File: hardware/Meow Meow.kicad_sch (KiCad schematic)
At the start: 33 parts

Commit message: update layout
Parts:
- removed C?: 1uF, Capacitor_SMD:C_0603_1608Metric, symbol Meow-Meow-rescue:C_Small-MeowMeow-Meow-Meow-rescue-Meow-Meow-rescue-Meow-Meow-r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
- removed C?: 0.1uF, Capacitor_SMD:C_0603_1608Metric, symbol Meow-Meow-rescue:C_Small-MeowMeow-Meow-Meow-rescue-Meow-Meow-rescue-Meow-Meow-r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
- removed L?: 50Ω at 20MHz and 220Ω at 100MHz, symbol Device:L
- L1: renamed from L?; LCSC# (none) -> C85840
- gave numbers to parts that had none: 2
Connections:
- net GPIO05: now also U1.29 (PA20), U3.29 (PA20); no longer U1.30 (PA21), U3.30 (PA21)
- net GPIO06: now also U1.30 (PA21), U3.30 (PA21); no longer U1.29 (PA20), U3.29 (PA20)
- net GPIO10: now also U1.23 (PA14), U3.23 (PA14); no longer U1.20 (PB11), U3.20 (PB11)
- net GPIO11: now also U1.20 (PB11), U3.20 (PB11); no longer U1.23 (PA14), U3.23 (PA14)
- net VDDCORE: now reaches C1.1, U3.41 (VDDCORE)
- net VDDCORE: now also U1.41 (VDDCORE)
- net VDDANA: now reaches U1.6 (VDDANA)
- net VDDANA: now also L1.2, U3.6 (VDDANA)
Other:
- note added: "GPIO5 change to GPIO6"

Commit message: update version
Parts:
- C1: value (none) -> 1uF; footprint (none) -> Capacitor_SMD:C_0603_1608Metric
- C2, C7: value (none) -> 0.1uF; footprint (none) -> Capacitor_SMD:C_0603_1608Metric
- C4, C6: value (none) -> 10uF; footprint (none) -> Capacitors_SMD:C_0805_HandSoldering
- C5: value (none) -> 0.1uF; footprint (none) -> Capacitors_SMD:C_0805_HandSoldering
- D1: value (none) -> POWER; footprint (none) -> LEDs:LED_0805_HandSoldering
- D2: value (none) -> LED; footprint (none) -> LEDs:LED_0805_HandSoldering
- F1: value (none) -> 0.5A; footprint (none) -> Resistors_SMD:R_1812_HandSoldering
- J1: value (none) -> Conn_Left; footprint (none) -> Connector_PinSocket_2.54mm:PinSocket_1x16_P2.54mm_Vertical_SMD_Pin1Left
- J2: value (none) -> Conn_Right; footprint (none) -> Connector_PinSocket_2.54mm:PinSocket_1x12_P2.54mm_Vertical_SMD_Pin1Right
- J3: value (none) -> Conn_01x06; footprint (none) -> Connector:Tag-Connect_TC2030-IDC-NL_2x03_P1.27mm_Vertical
- L1: value (none) -> 50Ω at 20MHz and 220Ω at 100MHz; footprint (none) -> Inductor_SMD:L_0805_2012Metric
- P1: value (none) -> SPACE; footprint (none) -> Connectors_EC:SEWALLI_renew
- P10: value (none) -> A; footprint (none) -> Connectors_EC:SEWALLI_renew
- P11: value (none) -> W; footprint (none) -> Connectors_EC:SEWALLI_renew
- P12: value (none) -> KEY_UP_ARROW; footprint (none) -> Connectors_EC:SEWALLI_renew
- P2: value (none) -> KEY_DOWN_ARROW; footprint (none) -> Connectors_EC:SEWALLI_renew
- P3: value (none) -> KEY_RIGHT_ARROW; footprint (none) -> Connectors_EC:SEWALLI_renew
- P5: value (none) -> KEY_LEFT_ARROW; footprint (none) -> Connectors_EC:SEWALLI_renew
- P6: value (none) -> D; footprint (none) -> Connectors_EC:SEWALLI_renew
- P7: value (none) -> S; footprint (none) -> Connectors_EC:SEWALLI_renew
- P8: value (none) -> MOUSE_LEFT; footprint (none) -> Connectors_EC:SEWALLI_renew
- P9: value (none) -> USB_Micro; footprint (none) -> Connectors:U254051N4BH806
- R2, R3: value (none) -> 1K; footprint (none) -> Resistors_SMD:R_0805_HandSoldering
- SW1: value (none) -> RESET; footprint (none) -> Buttons_Switches_SMD:SW_SPST_TL3342
- U1: value (none) -> ATSAML21G18B-MUT; footprint (none) -> Package_DFN_QFN:QFN-48-1EP_7x7mm_P0.5mm_EP5.15x5.15mm; DNP (none) -> YES; manf# (none) -> ATSAML21G18B-MUT
- U2: value (none) -> AP2114-HA; footprint (none) -> Package_TO_SOT_SMD:SOT-223
- U3: value (none) -> ATSAML21G18B-AUT; footprint (none) -> Package_QFP:TQFP-48_7x7mm_P0.5mm; manf# (none) -> ATSAML21G18B-AUT

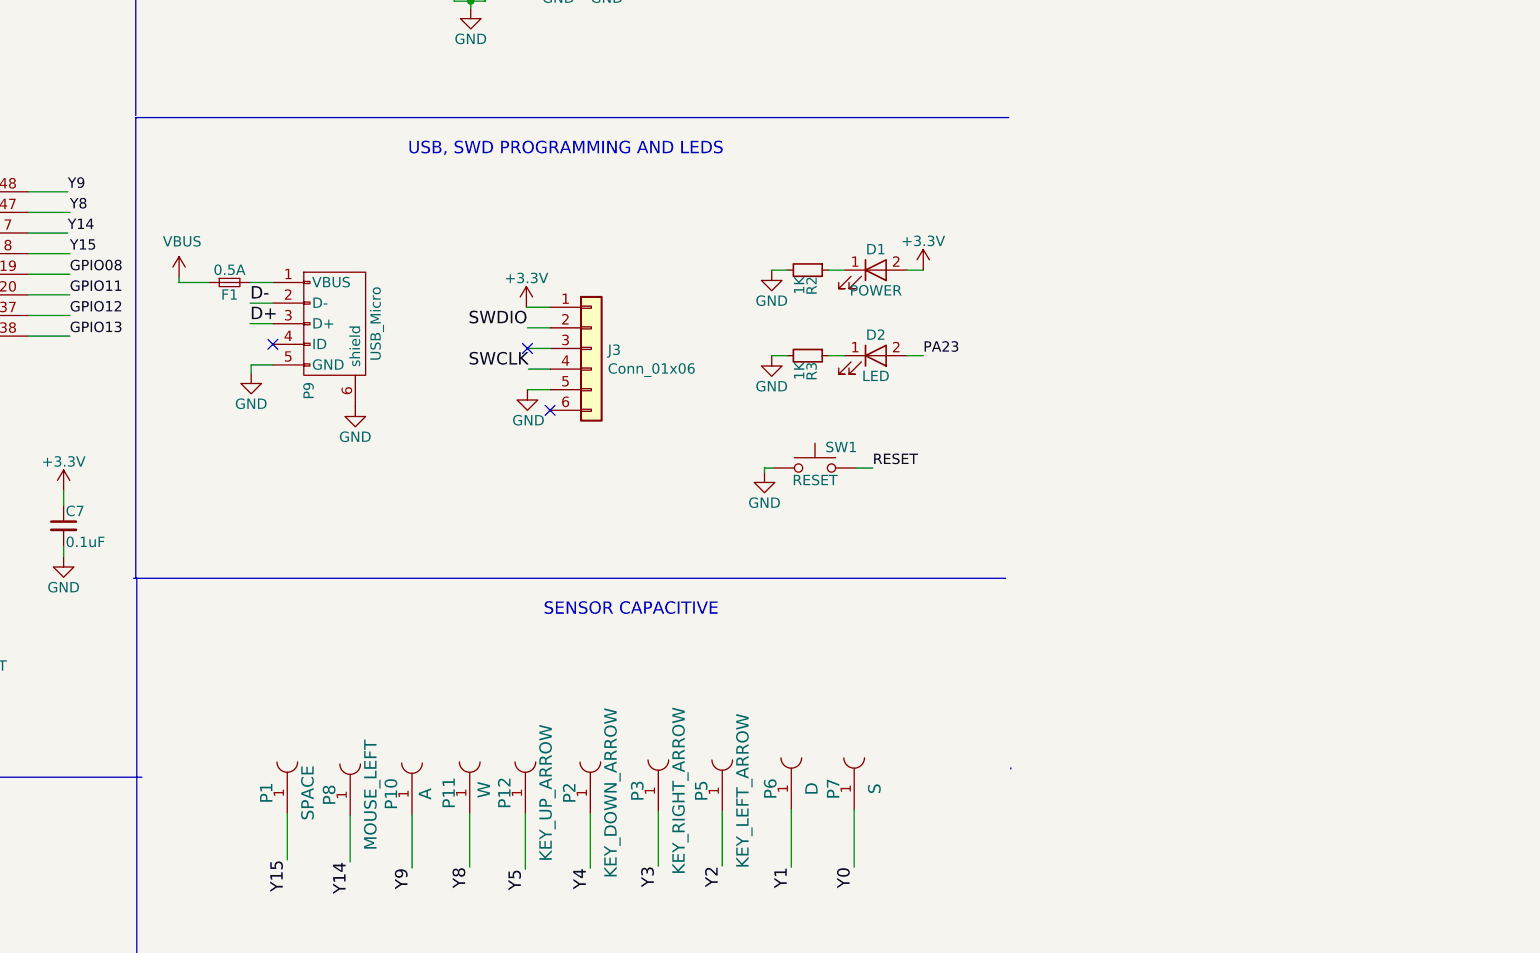
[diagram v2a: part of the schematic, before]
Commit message: update USB connector v3.1
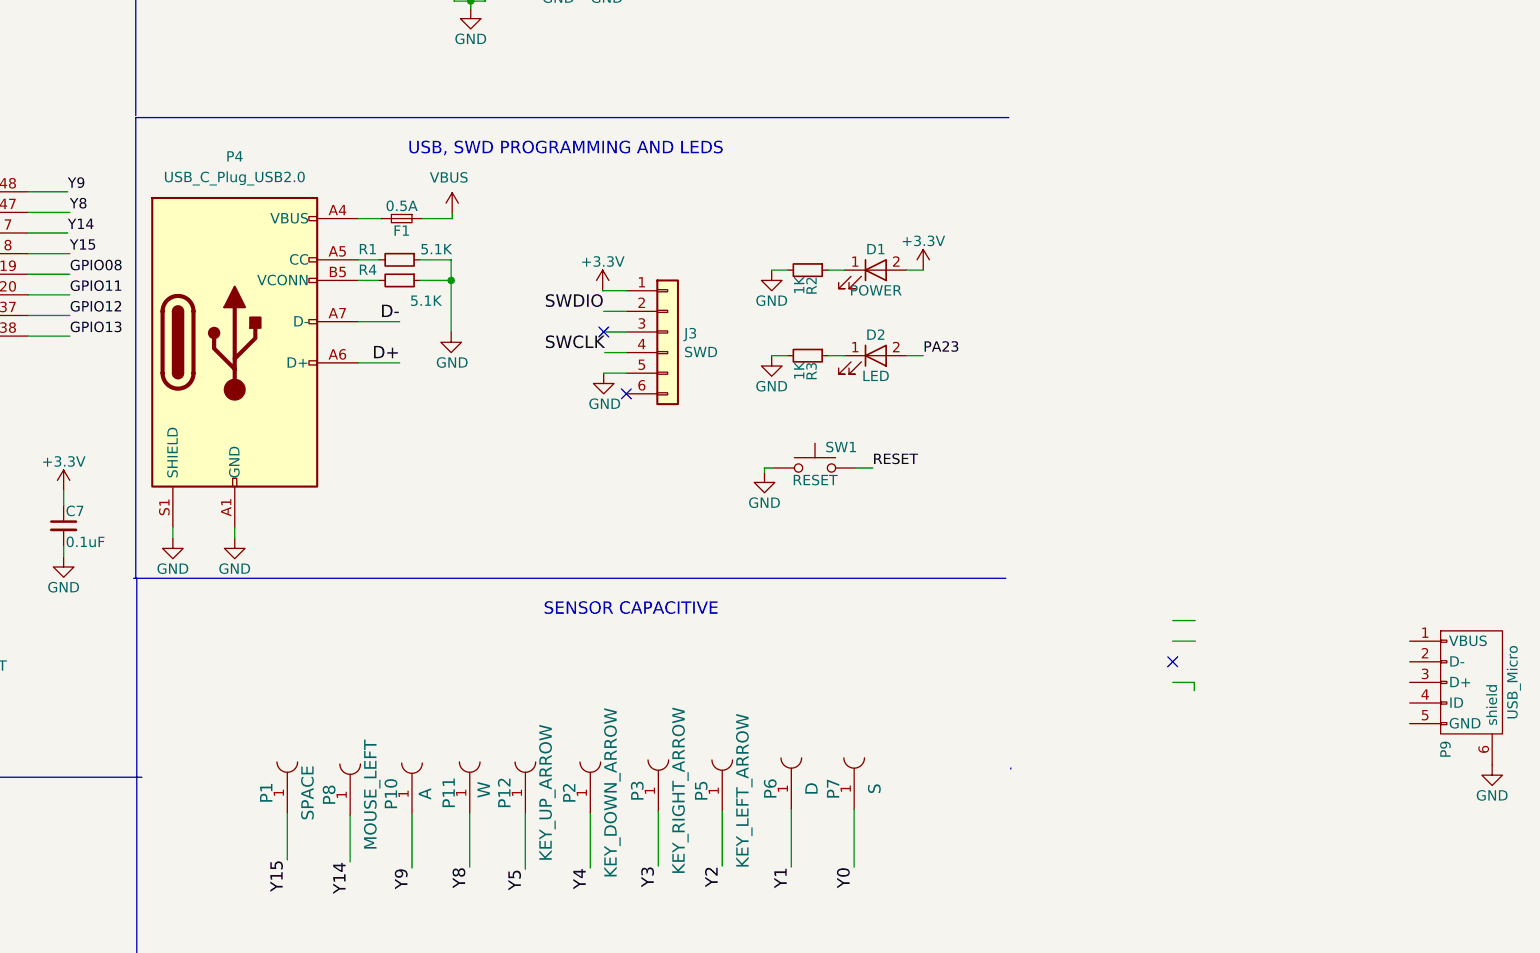
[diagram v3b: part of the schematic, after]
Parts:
- added P4: USB_C_Plug_USB2.0, Connectors:C393939, symbol Connector:USB_C_Plug_USB2.0
- added R1, R4: 5.1K, Resistor_SMD:R_0805_2012Metric, symbol Meow-Meow-rescue:R_Small-MeowMeow-Meow-Meow-rescue-Meow-Meow-rescue-Meow-Meow-r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
- J3: value Conn_01x06 -> SWD
- R2, R3: footprint Resistors_SMD:R_0805_HandSoldering -> Resistor_SMD:R_0805_2012Metric
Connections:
- net D+: now also P4.A6 (D+); no longer P9.3 (D+)
- net D-: now also P4.A7 (D-); no longer P9.2 (D-)
- net GND: now also P4.A1 (GND), P4.A12 (GND), P4.B1 (GND), P4.B12 (GND), P4.S1 (SHIELD), R1.1, R4.1; no longer P9.5 (GND)
- net at P9.1 (VBUS): no longer F1.2
- new net: F1.2, P4.A4 (VBUS), P4.A9 (VBUS), P4.B4 (VBUS), P4.B9 (VBUS)
- new net: P4.A5 (CC), R1.2
- new net: P4.B5 (VCONN), R4.2
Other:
- moved on the sheet: F1, J3, P9
